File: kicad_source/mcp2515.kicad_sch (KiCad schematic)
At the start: 14 parts, among them J5 BM04B-GHS-TBT, J6 BM04B-GHS-TBT, U2 MCP2515-I/SO, U3 SN65HVD232, Y1 RH100-16.000-16-3030-EXT-TR

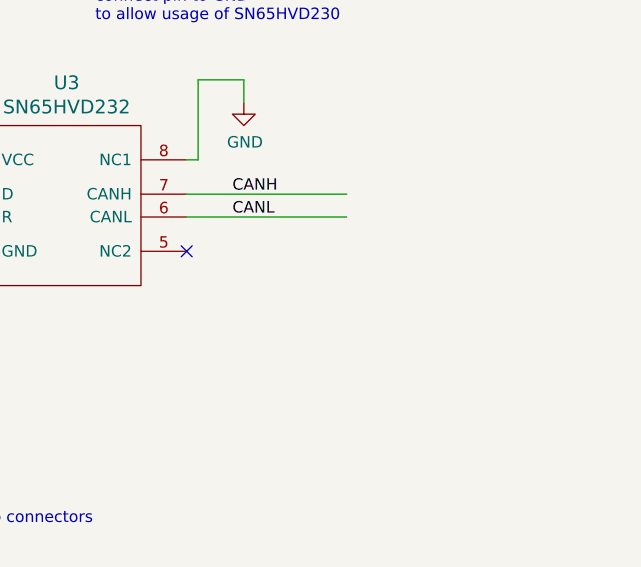
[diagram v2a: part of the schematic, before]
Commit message: added tvs diode on input
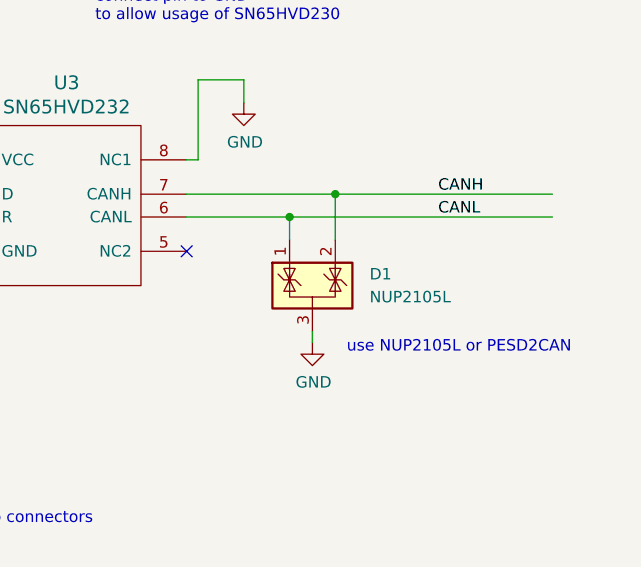
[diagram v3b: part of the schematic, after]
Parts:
- added D1: NUP2105L, Package_TO_SOT_SMD:SOT-23, symbol Power_Protection:NUP2105L
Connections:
- net CANH: now also D1.2 (K)
- net CANL: now also D1.1 (K)
- net GND: now also D1.3 (A)
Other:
- note added: "use NUP2105L or PESD2CAN"
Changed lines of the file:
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@@
   (junction (at 162.56 50.8) (diameter 0) (color 0 0 0 0)
   )
+  (junction (at 248.92 58.42) (diameter 0) (color 0 0 0 0)
+  )
   (junction (at 72.39 55.88) (diameter 0) (color 0 0 0 0)
   )
   (junction (at 163.83 81.28) (diameter 0) (color 0 0 0 0)
+  )
+  (junction (at 254 55.88) (diameter 0) (color 0 0 0 0)
   )
   (junction (at 176.53 81.28) (diameter 0) (color 0 0 0 0)
@@
     (stroke (width 0) (type default) (color 0 0 0 0))
   )
+  (wire (pts (xy 237.49 55.88) (xy 254 55.88))
+    (stroke (width 0) (type default) (color 0 0 0 0))
+  )
   (wire (pts (xy 168.91 85.09) (xy 170.18 85.09))
     (stroke (width 0) (type default) (color 0 0 0 0))
@@
     (stroke (width 0) (type default) (color 0 0 0 0))
   )
+  (wire (pts (xy 248.92 58.42) (xy 248.92 60.96))
+    (stroke (width 0) (type default) (color 0 0 0 0))
+  )
   (wire (pts (xy 209.55 62.23) (xy 209.55 63.5))
     (stroke (width 0) (type default) (color 0 0 0 0))
@@
     (stroke (width 0) (type default) (color 0 0 0 0))
   )
-  (wire (pts (xy 255.27 58.42) (xy 237.49 58.42))
+  (wire (pts (xy 237.49 58.42) (xy 248.92 58.42))
+    (stroke (width 0) (type default) (color 0 0 0 0))
+  )
+  (wire (pts (xy 254 55.88) (xy 254 60.96))
     (stroke (width 0) (type default) (color 0 0 0 0))
   )
@@
     (stroke (width 0) (type default) (color 0 0 0 0))
   )
+  (wire (pts (xy 251.46 71.12) (xy 251.46 72.39))
+    (stroke (width 0) (type default) (color 0 0 0 0))
+  )
   (wire (pts (xy 196.85 107.95) (xy 218.44 107.95))
     (stroke (width 0) (type default) (color 0 0 0 0))
@@
     (stroke (width 0) (type default) (color 0 0 0 0))
   )
-  (wire (pts (xy 255.27 55.88) (xy 237.49 55.88))
-    (stroke (width 0) (type default) (color 0 0 0 0))
-  )
   (wire (pts (xy 140.97 66.04) (xy 163.83 66.04))
     (stroke (width 0) (type default) (color 0 0 0 0))
   )
+  (wire (pts (xy 248.92 58.42) (xy 278.13 58.42))
+    (stroke (width 0) (type default) (color 0 0 0 0))
+  )
   (wire (pts (xy 196.85 102.87) (xy 218.44 102.87))
     (stroke (width 0) (type default) (color 0 0 0 0))
@@
     (stroke (width 0) (type default) (color 0 0 0 0))
   )
+  (wire (pts (xy 254 55.88) (xy 278.13 55.88))
+    (stroke (width 0) (type default) (color 0 0 0 0))
+  )
   (wire (pts (xy 140.97 58.42) (xy 210.82 58.42))
     (stroke (width 0) (type default) (color 0 0 0 0))
@@
     (effects (font (size 1.27 1.27)) (justify left bottom))
   )
+  (text "use NUP2105L or PESD2CAN" (at 255.27 73.66 0)
+    (effects (font (size 1.27 1.27)) (justify left bottom))
+  )
   (text "UCANPHY Micro connectors" (at 203.2 92.71 0)
     (effects (font (size 1.27 1.27)) (justify left bottom))
@@
     (effects (font (size 1.27 1.27)) (justify left bottom))
   )
-  (label "CANH" (at 242.57 55.88 0)
+  (label "CANH" (at 265.43 55.88 0)
     (effects (font (size 1.27 1.27)) (justify left bottom))
   )
@@
     (effects (font (size 1.27 1.27)) (justify left bottom))
   )
-  (label "CANL" (at 242.57 58.42 0)
+  (label "CANL" (at 265.43 58.42 0)
     (effects (font (size 1.27 1.27)) (justify left bottom))
   )
@@
     (pin "1")
   )
+  (symbol (lib_id "Power_Protection:NUP2105L") (at 251.46 66.04 0) (unit 1)
+    (in_bom yes) (on_board yes) (fields_autoplaced)
+    (property "Reference" "D1" (id 0) (at 257.81 64.7699 0)
+      (effects (font (size 1.27 1.27)) (justify left))
+    )
+    (property "Value" "NUP2105L" (id 1) (at 257.81 67.3099 0)
+      (effects (font (size 1.27 1.27)) (justify left))
+    )
+    (property "Footprint" "Package_TO_SOT_SMD:SOT-23" (id 2) (at 257.175 67.31 0)
+      (effects (font (size 1.27 1.27)) (justify left) hide)
+    )
+    (property "Datasheet" "http://www.onsemi.com/pub_link/Collateral/NUP2105L-D.PDF" (id 3) (at 254.635 62.865 0)
+      (effects (font (size 1.27 1.27)) hide)
+    )
+    (pin "3")
+    (pin "1")
+    (pin "2")
+  )
+  (symbol (lib_id "power:GND") (at 251.46 72.39 0) (unit 1)
+    (in_bom yes) (on_board yes)
+    (property "Reference" "#PWR019" (id 0) (at 251.46 78.74 0)
+      (effects (font (size 1.27 1.27)) hide)
+    )
+    (property "Value" "GND" (id 1) (at 251.587 76.7842 0))
+    (property "Footprint" "" (id 2) (at 251.46 72.39 0))
+    (property "Datasheet" "" (id 3) (at 251.46 72.39 0))
+    (pin "1")
+  )
